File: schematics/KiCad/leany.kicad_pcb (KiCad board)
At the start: 2 copper layers, 89.4 x 69 mm, 71 parts, among them J1 SWD, J2 ST7735S, J3 USB C, J4 BATT, Q1 AO3401A, Q2 DMG6601LVT-7, SW1 RESET, SW2 FLASH, SW3 ZERO, SW4 HOLD, SW5 POWER, U1 LSM6DSO, U2 STM32F103C8Tx, U3 CH340C, U4 AP2112K-3.3, U5 BQ25619, Y1 8MHz

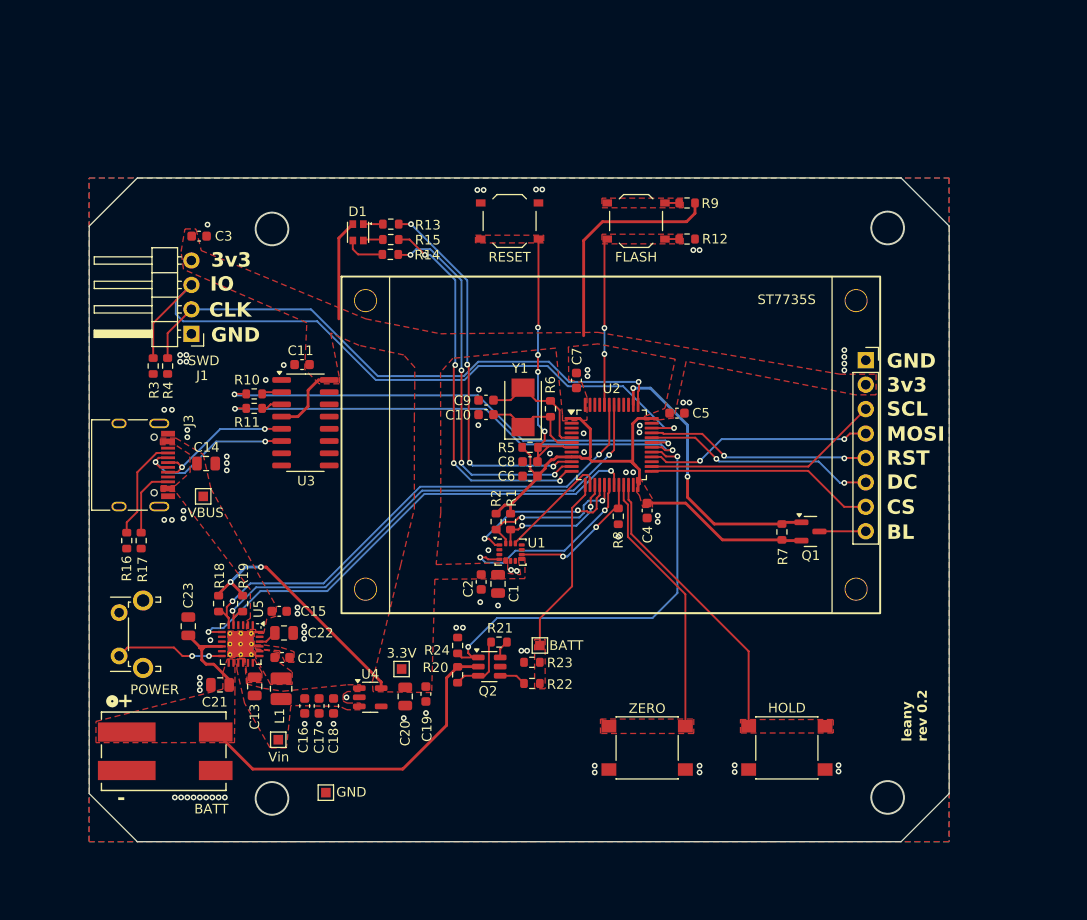
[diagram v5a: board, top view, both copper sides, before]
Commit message: implement a github action to generate production files Get rid of the JLCPCB plug-in Optimise JLCPCB pricing with components choice
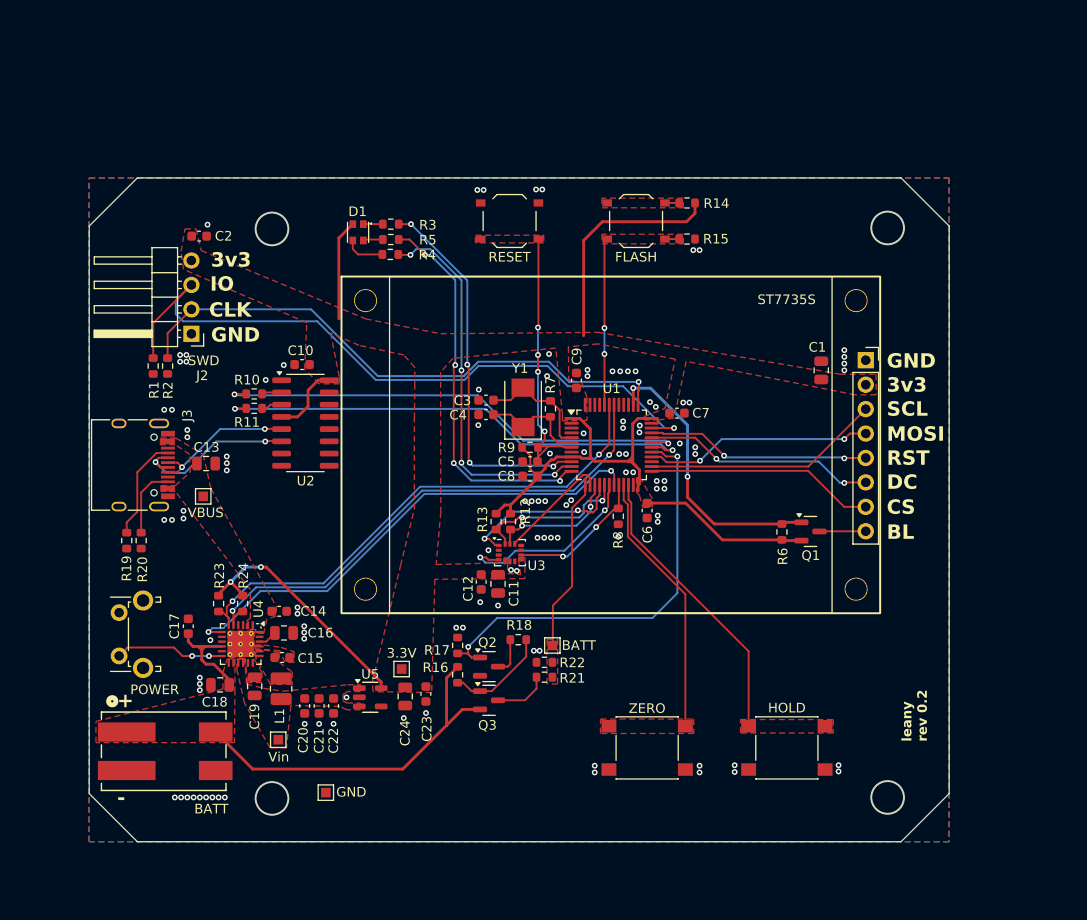
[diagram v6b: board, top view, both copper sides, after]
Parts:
- removed the U1 at (139.8, 111.4)
- added C1: 10u, Capacitor_SMD:C_0805_2012Metric, F.Cu at (172.1, 92.5)
- added Q3: AO3401A, Package_TO_SOT_SMD:SOT-23, F.Cu at (137.6, 126.8)
- added U2: CH340C, Package_SO:SOIC-16_3.9x9.9mm_P1.27mm, F.Cu at (118.5, 98.0)
- C17: renamed from C23; footprint Capacitor_SMD:C_0805_2012Metric -> Capacitor_SMD:C_0603_1608Metric
- Q2: value DMG6601LVT-7 -> AO3400A; footprint Package_TO_SOT_SMD:TSOT-23-6 -> Package_TO_SOT_SMD:SOT-23
- U3: value CH340C -> BMI270; footprint Package_SO:SOIC-16_3.9x9.9mm_P1.27mm -> Package_LGA:LGA-14_3x2.5mm_P0.5mm_LayoutBorder3x4y
- moved U3 25.2 mm to (139.7, 111.5)
- moved R18 2.02 mm to (140.6, 120.5), turned to 180 degrees
- moved R21 1.45 mm to (143.3, 124.4)
- moved TP3 1.30 mm to (144.2, 121.1)
- moved R22 1.30 mm to (143.3, 122.8)
- renumbered C11 to C10, C1 to C11, C2 to C12, C14 to C13, C15 to C14, C12 to C15, C22 to C16, C21 to C18, C13 to C19, C3 to C2, C16 to C20, C17 to C21, C18 to C22, C19 to C23, C20 to C24, C9 to C3, C10 to C4, C8 to C5, C4 to C6, C5 to C7, C6 to C8, C7 to C9, J2 to J1, J1 to J2, R3 to R1, R1 to R12, R2 to R13, R9 to R14, R12 to R15, R20 to R16, R24 to R17, R21 to R18, R16 to R19, R4 to R2, R17 to R20, R22 to R21, R23 to R22, R18 to R23, R19 to R24, R13 to R3, R14 to R4, R15 to R5, R7 to R6, R6 to R7, R5 to R9, SW3 to SW1, SW4 to SW2, SW1 to SW3, SW2 to SW4, TP4 to TP1, TP5 to TP3, TP1 to TP4, TP3 to TP5, U2 to U1, U5 to U4, U4 to U5
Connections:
- Q2 pad 2: +BATT -> GND
- Q2 pad 3: Net-(Q2B-G) -> Net-(Q2-D)
- R10 pad 2: Net-(U3-TXD) -> Net-(U2-TXD)
- R11 pad 2: Net-(U3-RXD) -> Net-(U2-RXD)
- R16 pad 1: Net-(Q2B-G) -> Net-(Q3-G)
- R18 pad 1: Net-(Q2B-G) -> Net-(Q3-G)
- R18 pad 2: Net-(Q2A-D) -> Net-(Q2-D)
- R21 pad 2: Net-(Q2B-D) -> Net-(Q3-D)
- U3 pad 1: GND -> /LSM6DSO_SDO
- U3 pad 12: unconnected-(U3-~{DCD}-Pad12) -> /LSM6DSO_CS
- U3 pad 13: unconnected-(U3-~{DTR}-Pad13) -> /LSM6DSO_SCL
- U3 pad 14: unconnected-(U3-~{RTS}-Pad14) -> /LSM6DSO_SDA
- U3 pad 2: Net-(U3-TXD) -> unconnected-(U3-ASDx-Pad2)
- U3 pad 3: Net-(U3-RXD) -> unconnected-(U3-ASCx-Pad3)
- U3 pad 4: +3V3 -> /LSM6DSO_INT1
- U3 pad 5: USB_D+ -> +3V3
- U3 pad 6: USB_D- -> GND
- U3 pad 7: unconnected-(U3-NC-Pad7) -> GND
- U3 pad 8: unconnected-(U3-NC-Pad8) -> +3V3
- U3 pad 9: unconnected-(U3-~{CTS}-Pad9) -> /LSM6DSO_INT2
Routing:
- net Net-(Q3-G): track 0.00 -> 10.7 mm
- net Net-(Q2B-G): track 6.89 -> 0.00 mm
- net Net-(Q3-D): track 0.00 -> 5.70 mm
- net Net-(Q2-D): track 0.00 -> 3.91 mm
- net Net-(Q2B-D): track 2.81 -> 0.00 mm
- net +BATT: track 45.9 -> 48.4 mm
- net Net-(U3-RXD): track 2.19 -> 0.00 mm
- net Net-(U2-RXD): track 0.00 -> 2.18 mm
- net Net-(U3-TXD): track 2.10 -> 0.00 mm
- net Net-(U2-TXD): track 0.00 -> 2.09 mm
- net Net-(Q2A-D): track 1.89 -> 0.00 mm
- net +3V3: track 121.9 -> 122.8 mm
- net BATT_VOLT: track 18.6 -> 18.1 mm
- net GND: vias 85 -> 114

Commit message: fix LED footprint
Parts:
- moved R4 3.00 mm to (127.3, 77.5)
- moved R3 1.65 mm to (127.3, 79.0)
- moved R5 1.55 mm to (127.3, 80.5)
- moved D1 0.16 mm to (123.9, 78.3), turned to 0 degrees
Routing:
- net Net-(D1-BK): track 2.07 -> 4.50 mm
- net Net-(D1-GK): track 4.20 -> 1.90 mm
- net /LED_BLUE: track 40.4 -> 38.9 mm
- net /LED_RED: track 39.6 -> 38.4 mm
- net /LED_GREEN: track 39.6 -> 40.5 mm
